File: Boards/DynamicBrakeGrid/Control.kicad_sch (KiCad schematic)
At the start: 47 parts, among them IC1 ISO1042BDWVR, IC5 LM358DR, IC6 MCP2515-e_ST, Y1 8MHz

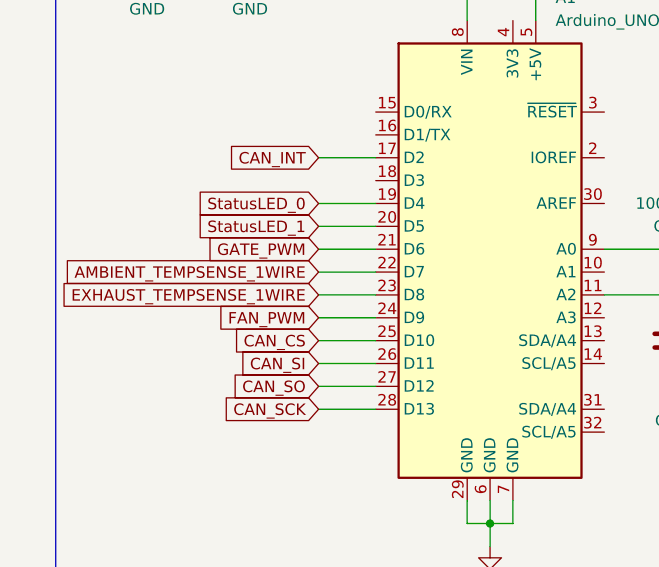
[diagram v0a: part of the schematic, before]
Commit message: Update Dynamic Brake Board
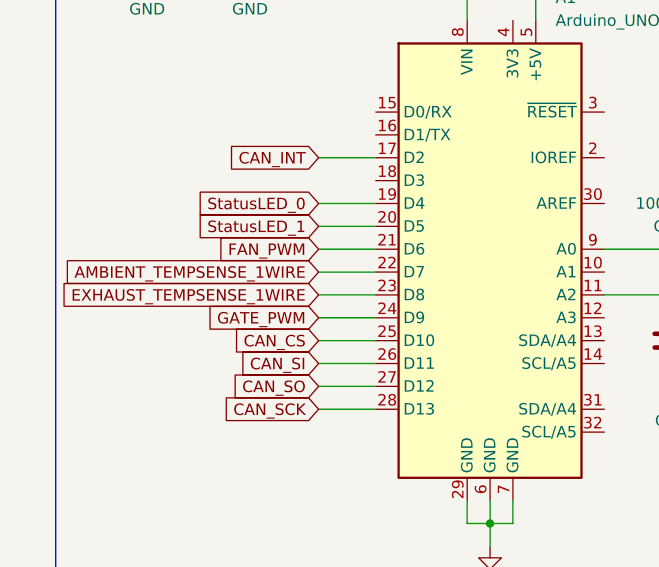
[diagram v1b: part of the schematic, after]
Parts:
- Y1: footprint Crystal:Crystal_SMD_7050-2Pin_7.0x5.0mm_HandSoldering -> Crystal:Crystal_HC49-4H_Vertical
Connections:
- net FAN_PWM: now also A1.21 (D6); no longer A1.24 (D9)
- net GATE_PWM: now also A1.24 (D9); no longer A1.21 (D6)
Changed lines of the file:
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@@
+		)
+	)
+	(global_label "GATE_PWM"
+		(shape input)
+		(at 43.18 67.31 180)
+		(fields_autoplaced yes)
+		(effects
+			(font
+				(size 1.27 1.27)
+			)
+			(justify right)
+		)
+		(property "Intersheetrefs" "${INTERSHEET_REFS}"
+			(at 30.5792 67.31 0)
+			(effects
+				(font
+					(size 1.27 1.27)
+				)
+				(justify right)
+				(hide yes)
+			)
 		)
 	)
@@
 		)
 	)
-	(global_label "GATE_PWM"
+	(global_label "CANBUS_ISO_GND"
+		(shape input)
+		(at 119.38 194.31 0)
+		(fields_autoplaced yes)
+		(effects
+			(font
+				(size 1.27 1.27)
+			)
+			(justify left)
+		)
+		(property "Intersheetrefs" "${INTERSHEET_REFS}"
+			(at 138.8148 194.31 0)
+			(effects
+				(font
+					(size 1.27 1.27)
+				)
+				(justify left)
+				(hide yes)
+			)
+		)
+	)
+	(global_label "CAN_SO"
+		(shape input)
+		(at 43.18 74.93 180)
+		(fields_autoplaced yes)
+		(effects
+			(font
+				(size 1.27 1.27)
+			)
+			(justify right)
+		)
+		(property "Intersheetrefs" "${INTERSHEET_REFS}"
+			(at 32.9981 74.93 0)
+			(effects
+				(font
+					(size 1.27 1.27)
+				)
+				(justify right)
+				(hide yes)
+			)
+		)
+	)
+	(global_label "CAN_SI"
+		(shape input)
+		(at 43.18 72.39 180)
+		(fields_autoplaced yes)
+		(effects
+			(font
+				(size 1.27 1.27)
+			)
+			(justify right)
+		)
+		(property "Intersheetrefs" "${INTERSHEET_REFS}"
+			(at 33.7238 72.39 0)
+			(effects
+				(font
+					(size 1.27 1.27)
+				)
+				(justify right)
+				(hide yes)
+			)
+		)
+	)
+	(global_label "CAN_SCK"
+		(shape input)
+		(at 43.18 77.47 180)
+		(fields_autoplaced yes)
+		(effects
+			(font
+				(size 1.27 1.27)
+			)
+			(justify right)
+		)
+		(property "Intersheetrefs" "${INTERSHEET_REFS}"
+			(at 31.7886 77.47 0)
+			(effects
+				(font
+					(size 1.27 1.27)
+				)
+				(justify right)
+				(hide yes)
+			)
+		)
+	)
+	(global_label "CAN_CS"
+		(shape input)
+		(at 93.98 128.27 0)
+		(fields_autoplaced yes)
+		(effects
+			(font
+				(size 1.27 1.27)
+			)
+			(justify left)
+		)
+		(property "Intersheetrefs" "${INTERSHEET_REFS}"
+			(at 104.1014 128.27 0)
+			(effects
+				(font
+					(size 1.27 1.27)
+				)
+				(justify left)
+				(hide yes)
+			)
+		)
+	)
+	(global_label "+12V"
+		(shape input)
+		(at 162.56 86.36 180)
+		(fields_autoplaced yes)
+		(effects
+			(font
+				(size 1.27 1.27)
+			)
+			(justify right)
+		)
+		(property "Intersheetrefs" "${INTERSHEET_REFS}"
+			(at 154.4948 86.36 0)
+			(effects
+				(font
+					(size 1.27 1.27)
+				)
+				(justify right)
+				(hide yes)
+			)
+		)
+	)
+	(global_label "FAN_PWM"
 		(shape input)
 		(at 43.18 59.69 180)
@@
 		)
 		(property "Intersheetrefs" "${INTERSHEET_REFS}"
-			(at 30.5792 59.69 0)
-			(effects
-				(font
-					(size 1.27 1.27)
-				)
-				(justify right)
-				(hide yes)
-			)
-		)
-	)
-	(global_label "CANBUS_ISO_GND"
-		(shape input)
-		(at 119.38 194.31 0)
-		(fields_autoplaced yes)
-		(effects
-			(font
-				(size 1.27 1.27)
-			)
-			(justify left)
-		)
-		(property "Intersheetrefs" "${INTERSHEET_REFS}"
-			(at 138.8148 194.31 0)
-			(effects
-				(font
-					(size 1.27 1.27)
-				)
-				(justify left)
-				(hide yes)
-			)
-		)
-	)
-	(global_label "CAN_SO"
-		(shape input)
-		(at 43.18 74.93 180)
-		(fields_autoplaced yes)
-		(effects
-			(font
-				(size 1.27 1.27)
-			)
-			(justify right)
-		)
-		(property "Intersheetrefs" "${INTERSHEET_REFS}"
-			(at 32.9981 74.93 0)
-			(effects
-				(font
-					(size 1.27 1.27)
-				)
-				(justify right)
-				(hide yes)
-			)
-		)
-	)
-	(global_label "CAN_SI"
-		(shape input)
-		(at 43.18 72.39 180)
-		(fields_autoplaced yes)
-		(effects
-			(font
-				(size 1.27 1.27)
-			)
-			(justify right)
-		)
-		(property "Intersheetrefs" "${INTERSHEET_REFS}"
-			(at 33.7238 72.39 0)
-			(effects
-				(font
-					(size 1.27 1.27)
-				)
-				(justify right)
-				(hide yes)
-			)
-		)
-	)
-	(global_label "CAN_SCK"
-		(shape input)
-		(at 43.18 77.47 180)
-		(fields_autoplaced yes)
-		(effects
-			(font
-				(size 1.27 1.27)
-			)
-			(justify right)
-		)
-		(property "Intersheetrefs" "${INTERSHEET_REFS}"
-			(at 31.7886 77.47 0)
-			(effects
-				(font
-					(size 1.27 1.27)
-				)
-				(justify right)
-				(hide yes)
-			)
-		)
-	)
-	(global_label "CAN_CS"
-		(shape input)
-		(at 93.98 128.27 0)
-		(fields_autoplaced yes)
-		(effects
-			(font
-				(size 1.27 1.27)
-			)
-			(justify left)
-		)
-		(property "Intersheetrefs" "${INTERSHEET_REFS}"
-			(at 104.1014 128.27 0)
-			(effects
-				(font
-					(size 1.27 1.27)
-				)
-				(justify left)
-				(hide yes)
-			)
-		)
-	)
-	(global_label "+12V"
-		(shape input)
-		(at 162.56 86.36 180)
-		(fields_autoplaced yes)
-		(effects
-			(font
-				(size 1.27 1.27)
-			)
-			(justify right)
-		)
-		(property "Intersheetrefs" "${INTERSHEET_REFS}"
-			(at 154.4948 86.36 0)
-			(effects
-				(font
-					(size 1.27 1.27)
-				)
-				(justify right)
-				(hide yes)
-			)
-		)
-	)
-	(global_label "FAN_PWM"
-		(shape input)
-		(at 43.18 67.31 180)
-		(fields_autoplaced yes)
-		(effects
-			(font
-				(size 1.27 1.27)
-			)
-			(justify right)
-		)
-		(property "Intersheetrefs" "${INTERSHEET_REFS}"
-			(at 31.5467 67.31 0)
+			(at 31.5467 59.69 0)
 			(effects
 				(font
@@
 			)
 		)
-		(property "Footprint" "Crystal:Crystal_SMD_7050-2Pin_7.0x5.0mm_HandSoldering"
+		(property "Footprint" "Crystal:Crystal_HC49-4H_Vertical"
 			(at 33.02 143.51 0)
 			(effects

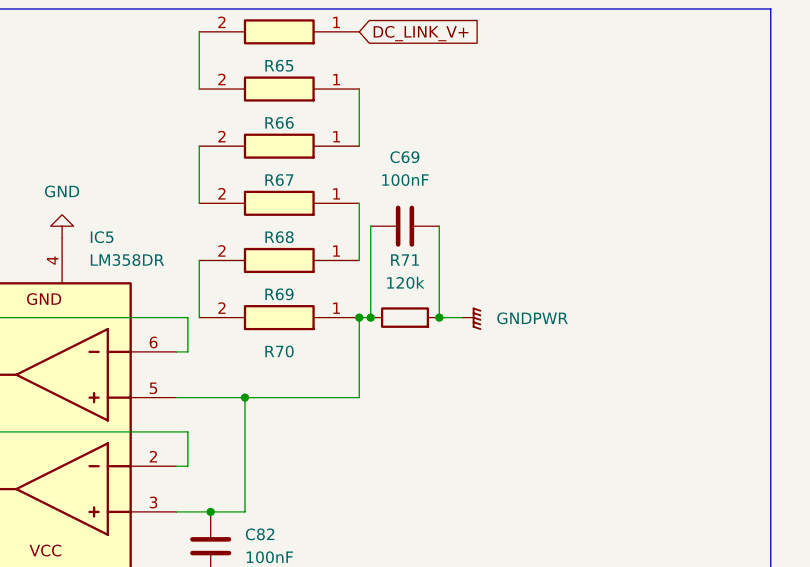
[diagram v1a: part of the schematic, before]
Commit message: Generate Bill of Materials
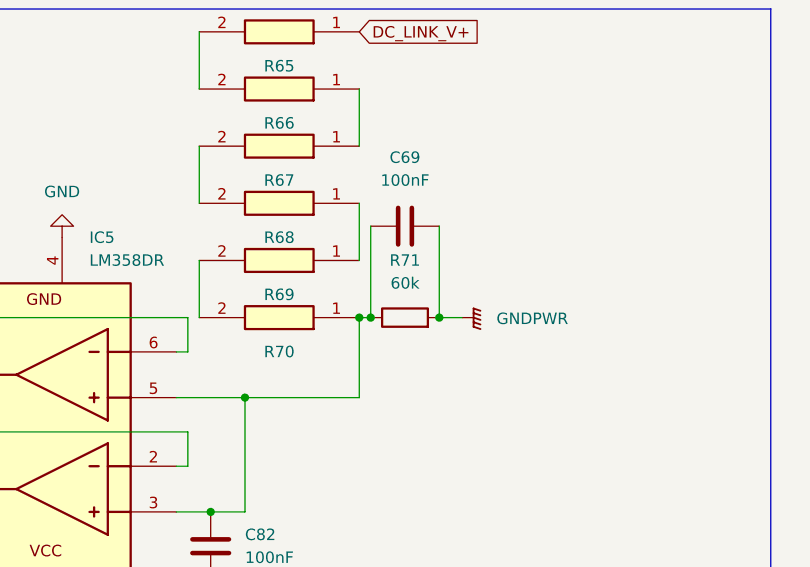
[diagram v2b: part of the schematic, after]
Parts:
- R71: value 120k -> 60k
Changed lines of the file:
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@@
 			)
 		)
-		(property "Value" "120k"
+		(property "Value" "60k"
 			(at 212.09 44.45 90)
 			(effects

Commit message: Update Dybrk FW
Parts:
- added C88: 1uF, Capacitor_SMD:C_1210_3225Metric_Pad1.33x2.70mm_HandSolder, symbol Device:C
- C69: value 100nF -> 100pF
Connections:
- net Arduino_VInSense: now also C88.2
- net GND: now also C88.1
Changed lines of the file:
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@@
 	(wire
 		(pts
+			(xy 138.43 59.69) (xy 138.43 60.96)
+		)
+		(stroke
+			(width 0)
+			(type default)
+		)
+	)
+	(wire
+		(pts
 			(xy 160.02 54.61) (xy 161.29 54.61)
 		)
@@
 	)
 	(symbol
+		(lib_id "power:GND")
+		(at 138.43 52.07 180)
+		(unit 1)
+		(exclude_from_sim no)
+		(in_bom yes)
+		(on_board yes)
+		(dnp no)
+		(fields_autoplaced yes)
+		(property "Reference" "#PWR079"
+			(at 138.43 45.72 0)
+			(effects
+				(font
+					(size 1.27 1.27)
+				)
+				(hide yes)
+			)
+		)
+		(property "Value" "GND"
+			(at 138.43 46.99 0)
+			(effects
+				(font
+					(size 1.27 1.27)
+				)
+			)
+		)
+		(property "Footprint" ""
+			(at 138.43 52.07 0)
+			(effects
+				(font
+					(size 1.27 1.27)
+				)
+				(hide yes)
+			)
+		)
+		(property "Datasheet" ""
+			(at 138.43 52.07 0)
+			(effects
+				(font
+					(size 1.27 1.27)
+				)
+				(hide yes)
+			)
+		)
+		(property "Description" "Power symbol creates a global label with name \"GND\" , ground"
+			(at 138.43 52.07 0)
+			(effects
+				(font
+					(size 1.27 1.27)
+				)
+				(hide yes)
+			)
+		)
+		(pin "1"
+		)
+		(instances
+			(project "DynamicBrakeGrid"
+				(path "/c99e0392-d1c3-4f46-a25d-449c454a3f3b/d6e0f048-8a0f-4eb8-baf0-22a230009567"
+					(reference "#PWR079")
+					(unit 1)
+				)
+			)
+		)
+	)
+	(symbol
 		(lib_id "MCU_Module:Arduino_UNO_R3")
 		(at 62.23 59.69 0)
@@
 	(symbol
 		(lib_id "Device:C")
+		(at 138.43 55.88 0)
+		(unit 1)
+		(exclude_from_sim no)
+		(in_bom yes)
+		(on_board yes)
+		(dnp no)
+		(fields_autoplaced yes)
+		(property "Reference" "C88"
+			(at 142.24 54.6099 0)
+			(effects
+				(font
+					(size 1.27 1.27)
+				)
+				(justify left)
+			)
+		)
+		(property "Value" "1uF"
+			(at 142.24 57.1499 0)
+			(effects
+				(font
+					(size 1.27 1.27)
+				)
+				(justify left)
+			)
+		)
+		(property "Footprint" "Capacitor_SMD:C_1210_3225Metric_Pad1.33x2.70mm_HandSolder"
+			(at 139.3952 59.69 0)
+			(effects
+				(font
+					(size 1.27 1.27)
+				)
+				(hide yes)
+			)
+		)
+		(property "Datasheet" "~"
+			(at 138.43 55.88 0)
+			(effects
+				(font
+					(size 1.27 1.27)
+				)
+				(hide yes)
+			)
+		)
+		(property "Description" "Unpolarized capacitor"
+			(at 138.43 55.88 0)
+			(effects
+				(font
+					(size 1.27 1.27)
+				)
+				(hide yes)
+			)
+		)
+		(pin "1"
+		)
+		(pin "2"
+		)
+		(instances
+			(project "DynamicBrakeGrid"
+				(path "/c99e0392-d1c3-4f46-a25d-449c454a3f3b/d6e0f048-8a0f-4eb8-baf0-22a230009567"
+					(reference "C88")
+					(unit 1)
+				)
+			)
+		)
+	)
+	(symbol
+		(lib_id "Device:C")
 		(at 77.47 172.72 90)
 		(unit 1)
@@
 			)
 		)
-		(property "Value" "100nF"
+		(property "Value" "100pF"
 			(at 212.09 33.02 90)
 			(effects
